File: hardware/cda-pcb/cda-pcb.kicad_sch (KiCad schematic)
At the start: 194 parts, among them J1 ICD15S13E4GX00LF, J2 ICD15S13E4GX00LF, J3 ICD15S13E4GX00LF, J4 ICD15S13E4GX00LF, J5 Conn_01x06, P1 436500227, U1 ADS124S08IRHBT, U10 SN74AHCT125RGYR, U2 ADS124S08IRHBT, U3 ADS124S08IRHBT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

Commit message: changed LS3 to FM1 and FM2
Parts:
- removed C9: 3.3nF, Capacitor_SMD:C_0603_1608Metric, symbol Device:C
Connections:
- net LS3_SIG+: no longer J3.6, R15.1
- net LS3_SIG-: no longer J3.11, R16.1
- new net FM1_SIG: J3.6, R15.1
- new net FM2_SIG: J3.11, R16.1
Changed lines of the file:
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@@
 	)
 	(junction
-		(at 66.04 128.27)
-		(diameter 0)
-		(color 0 0 0 0)
-	)
-	(junction
 		(at 133.35 154.94)
 		(diameter 0)
@@
 	)
 	(junction
-		(at 66.04 120.65)
-		(diameter 0)
-		(color 0 0 0 0)
-	)
-	(junction
 		(at 90.17 104.14)
 		(diameter 0)
@@
 	(wire
 		(pts
-			(xy 86.36 128.27) (xy 66.04 128.27)
+			(xy 62.23 128.27) (xy 86.36 128.27)
 		)
 		(stroke
@@
 	(wire
 		(pts
-			(xy 62.23 128.27) (xy 66.04 128.27)
-		)
-		(stroke
-			(width 0)
-			(type default)
-		)
-	)
-	(wire
-		(pts
 			(xy 416.56 354.33) (xy 426.72 354.33)
 		)
@@
 		)
 	)
-	(label "LS3_SIG-"
+	(label "FM2_SIG"
 		(at 41.91 128.27 0)
 		(effects
@@
 		)
 	)
-	(label "LS3_SIG-"
+	(label "FM2_SIG"
 		(at 400.05 344.17 0)
 		(effects
@@
 		)
 	)
-	(label "LS3_SIG+"
+	(label "FM1_SIG"
 		(at 41.91 120.65 0)
 		(effects
@@
 		)
 	)
-	(label "LS3_SIG+"
+	(label "FM1_SIG"
 		(at 364.49 359.41 0)
 		(effects
@@
 					(unit 1)
 				)
-			)
-		)
-	)
-	(symbol
-		(lib_id "Device:C")
-		(at 66.04 124.46 0)
-		(unit 1)
-		(exclude_from_sim no)
-		(in_bom yes)
-		(on_board yes)
-		(dnp no)
-		(property "Reference" "C9"
-			(at 68.834 123.19 0)
-			(effects
-				(font
-					(size 1.27 1.27)
-				)
-				(justify left)
-			)
-		)
-		(property "Value" "3.3nF"
-			(at 68.326 124.968 0)
-			(effects
-				(font
-					(size 1.27 1.27)
-				)
-				(justify left)
-			)
-		)
-		(property "Footprint" "Capacitor_SMD:C_0603_1608Metric"
-			(at 67.0052 128.27 0)
-			(effects
-				(font
-					(size 1.27 1.27)
-				)
-				(hide yes)
-			)
-		)
-		(property "Datasheet" "~"
-			(at 66.04 124.46 0)
-			(effects
-				(font
-					(size 1.27 1.27)
-				)
-				(hide yes)
-			)
-		)
-		(property "Description" "Unpolarized capacitor"
-			(at 66.04 124.46 0)
-			(effects
-				(font
-					(size 1.27 1.27)
-				)
-				(hide yes)
-			)
-		)
-		(pin "1"
-		)
-		(pin "2"
-		)
-		(instances
-			(project "DAQ"
-				(path "/98ce85a8-ddff-4ecb-9668-dd271ba07a43"
-					(reference "C9")
-					(unit 1)
-				)

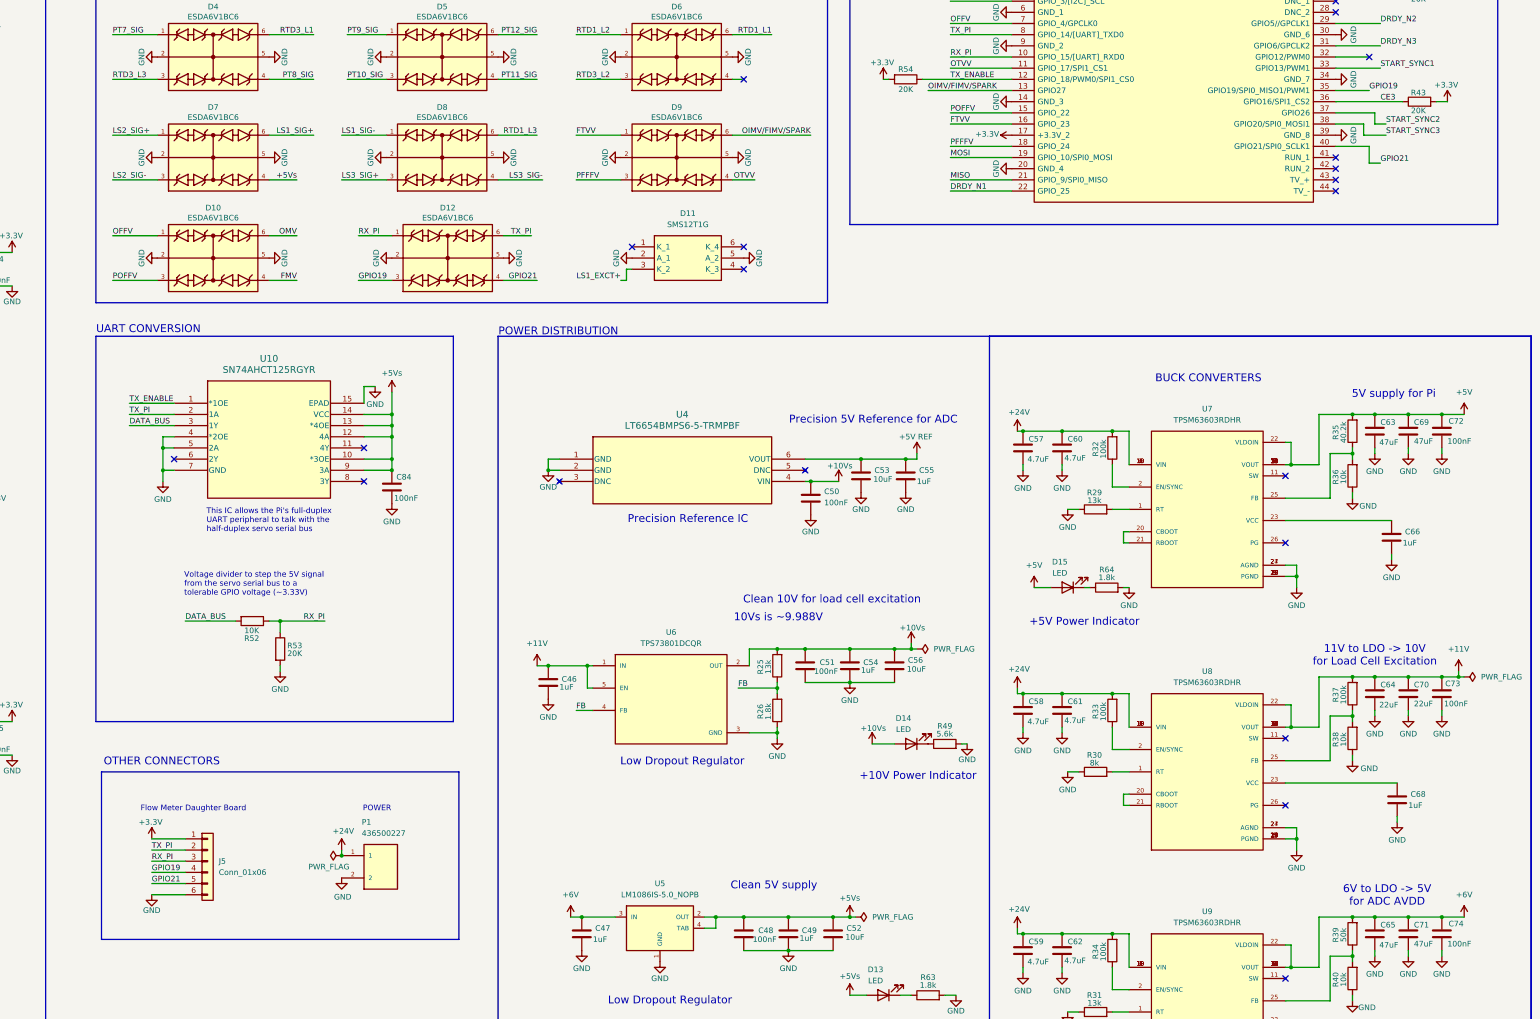
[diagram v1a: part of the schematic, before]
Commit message: swapped LS3 for FM1 & FM2 signals on ADC
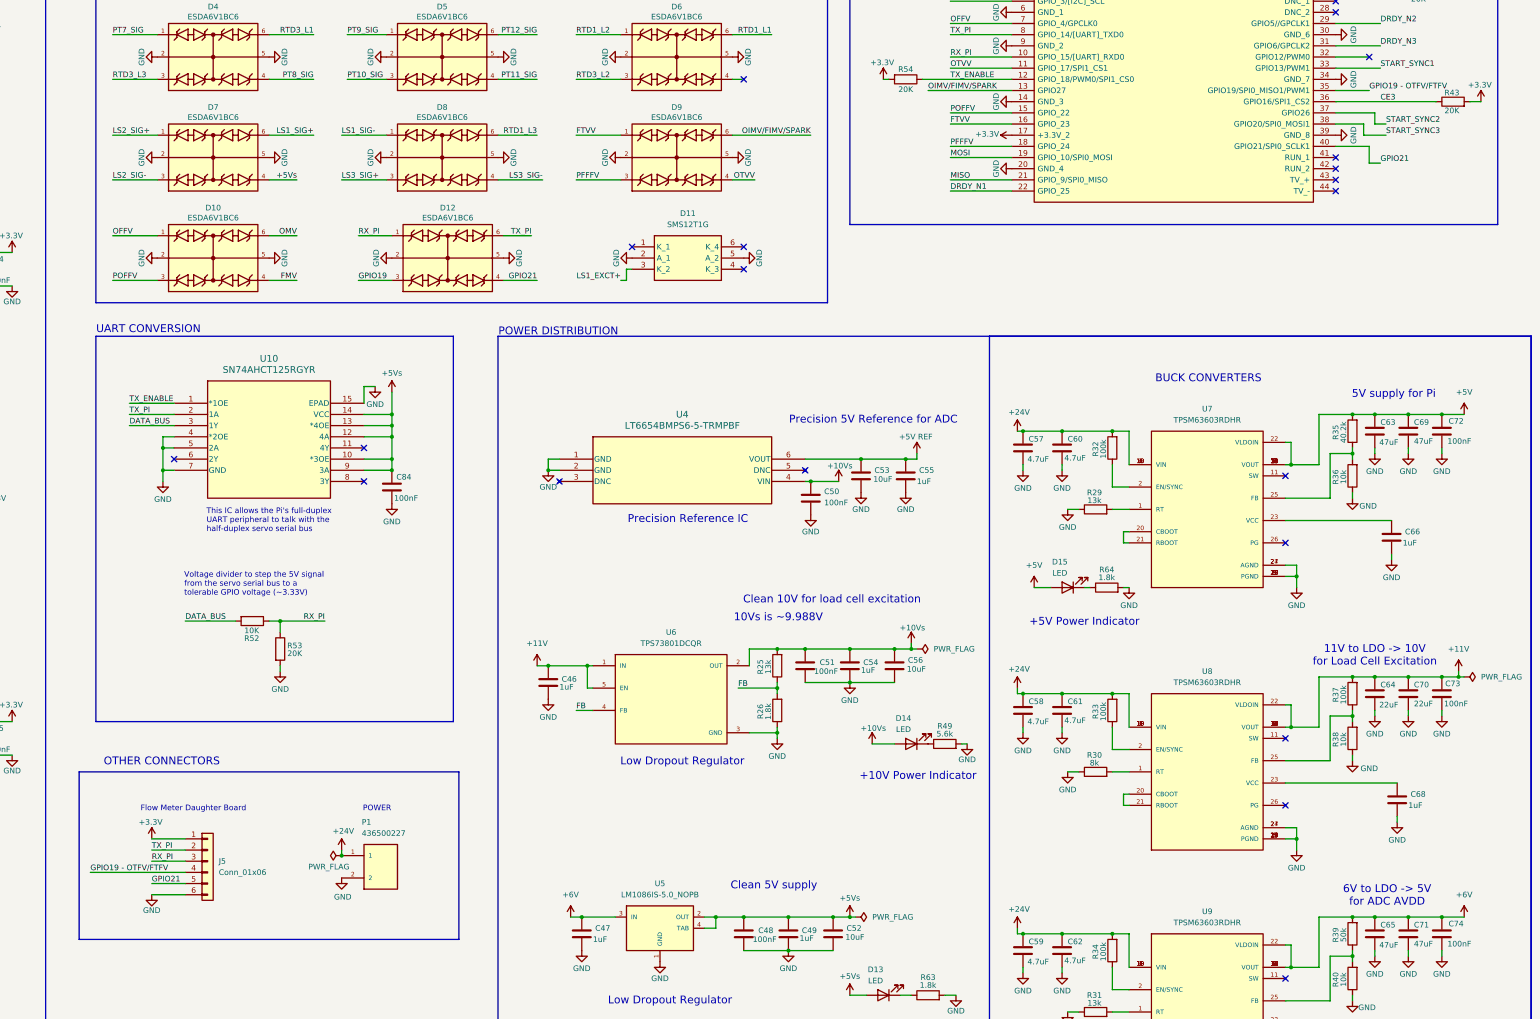
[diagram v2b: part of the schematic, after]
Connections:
- net GPIO19: no longer J5.4 (Pin_4), RP1.35 (GPIO19/SPI0_MISO1/PWM1)
- new net GPIO19 - OTFV/FTFV: J5.4 (Pin_4), RP1.35 (GPIO19/SPI0_MISO1/PWM1)
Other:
- moved on the sheet: R43
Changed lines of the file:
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@@
 	)
 	(rectangle
-		(start 254 234.95)
+		(start 248.92 234.95)
 		(end 335.28 273.05)
 		(stroke
@@
 	(wire
 		(pts
-			(xy 557.53 82.55) (xy 560.07 82.55)
+			(xy 565.15 82.55) (xy 567.69 82.55)
 		)
 		(stroke
@@
 	(wire
 		(pts
-			(xy 534.67 82.55) (xy 549.91 82.55)
+			(xy 534.67 82.55) (xy 557.53 82.55)
 		)
 		(stroke
@@
 	(wire
 		(pts
-			(xy 265.43 257.81) (xy 273.05 257.81)
+			(xy 251.46 257.81) (xy 273.05 257.81)
 		)
 		(stroke
@@
 		)
 	)
-	(label "GPIO19"
+	(label "GPIO19 - OTFV{slash}FTFV"
 		(at 542.29 80.01 0)
 		(effects
@@
 		)
 	)
-	(label "GPIO19"
-		(at 265.43 257.81 0)
+	(label "GPIO19 - OTFV{slash}FTFV"
+		(at 251.46 257.81 0)
 		(effects
 			(font
@@
 	(symbol
 		(lib_id "power:+3.3V")
-		(at 560.07 82.55 0)
+		(at 567.69 82.55 0)
 		(unit 1)
 		(exclude_from_sim no)
@@
 		(dnp no)
 		(property "Reference" "#PWR066"
-			(at 560.07 86.36 0)
+			(at 567.69 86.36 0)
 			(effects
 				(font
@@
 		)
 		(property "Value" "+3.3V"
-			(at 559.816 78.74 0)
+			(at 567.436 78.74 0)
 			(effects
 				(font
@@
 		)
 		(property "Footprint" ""
-			(at 560.07 82.55 0)
+			(at 567.69 82.55 0)
 			(effects
 				(font
@@
 		)
 		(property "Datasheet" ""
-			(at 560.07 82.55 0)
+			(at 567.69 82.55 0)
 			(effects
 				(font
@@
 		)
 		(property "Description" "Power symbol creates a global label with name \"+3.3V\""
-			(at 560.07 82.55 0)
+			(at 567.69 82.55 0)
 			(effects
 				(font
@@
 	(symbol
 		(lib_id "Device:R")
-		(at 553.72 82.55 90)
+		(at 561.34 82.55 90)
 		(unit 1)
 		(exclude_from_sim no)
@@
 		(dnp no)
 		(property "Reference" "R43"
-			(at 553.466 80.518 90)
+			(at 561.086 80.518 90)
 			(effects
 				(font
@@
 		)
 		(property "Value" "20K"
-			(at 553.466 84.582 90)
+			(at 561.086 84.582 90)
 			(effects
 				(font
@@
 		)
 		(property "Footprint" "CRCW060320K0FKEA:RESC1508X50N"
-			(at 553.72 84.328 90)
+			(at 561.34 84.328 90)
 			(effects
 				(font
@@
 		)
 		(property "Datasheet" "~"
-			(at 553.72 82.55 0)
+			(at 561.34 82.55 0)
 			(effects
 				(font
@@
 		)
 		(property "Description" "Resistor"
-			(at 553.72 82.55 0)
+			(at 561.34 82.55 0)
 			(effects
 				(font
